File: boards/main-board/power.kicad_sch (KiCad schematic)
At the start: 18 parts, among them U3 LM317

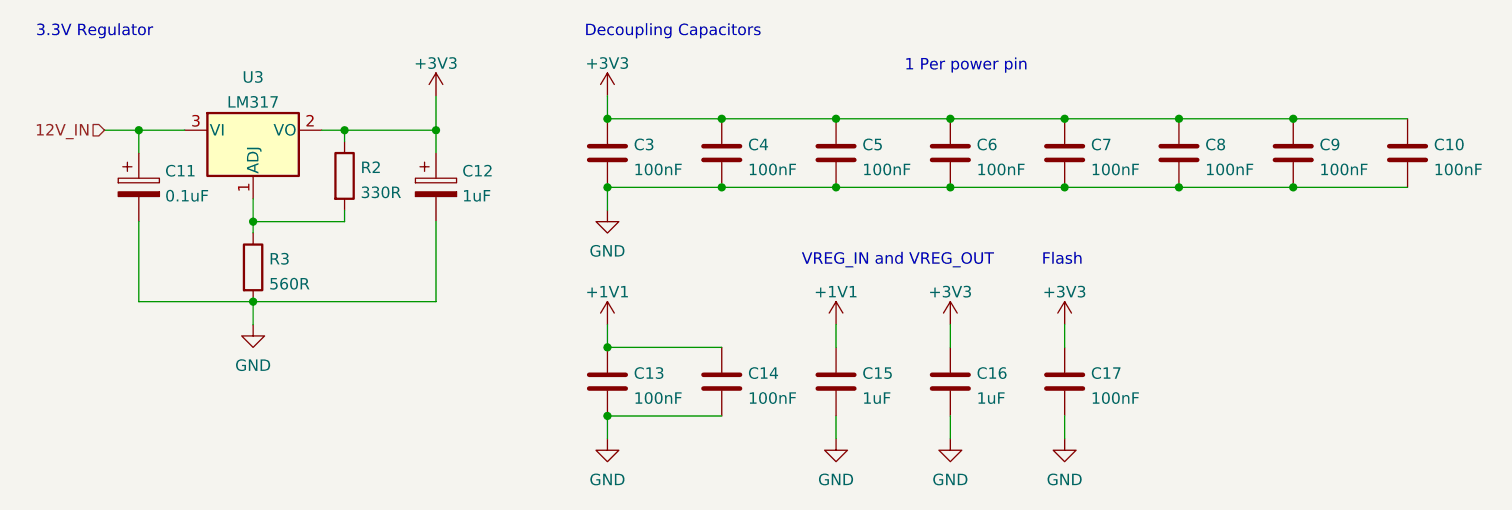
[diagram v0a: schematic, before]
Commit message: Version 1.1.0 of main control board schematic
Signed-off-by: Computroniks <mnickson@sidingsmedia.com>
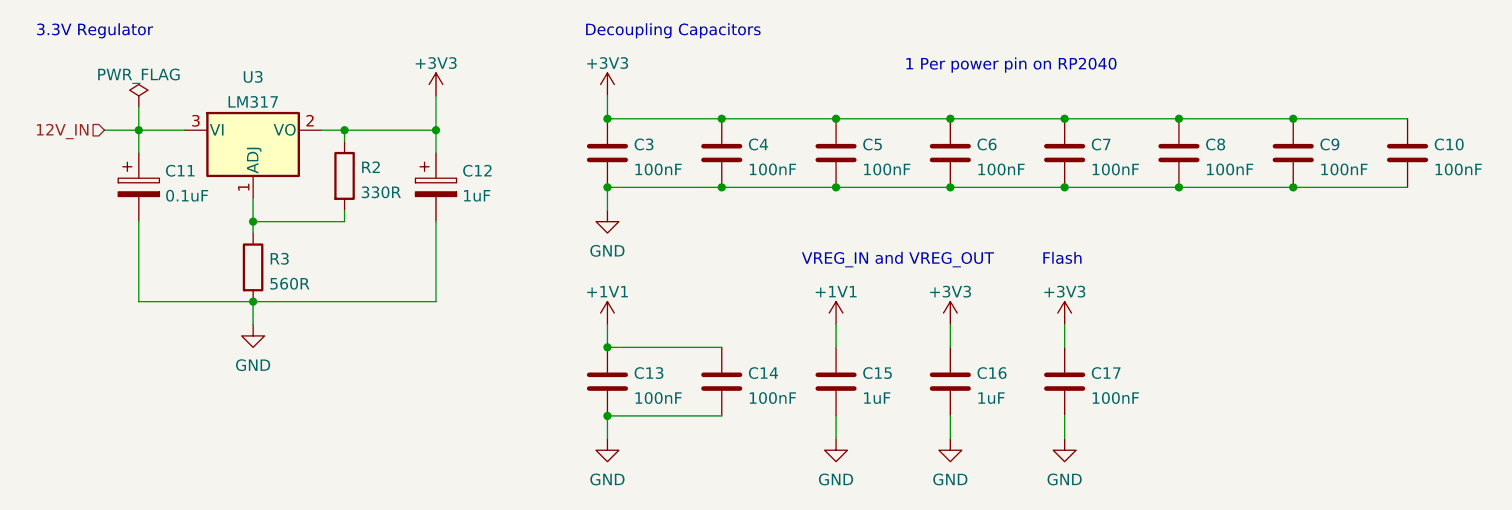
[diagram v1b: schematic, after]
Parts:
- C10, C13, C14, C15, C16, C17, C3, C4, C5, C6, C7, C8, C9: footprint (none) -> Capacitor_SMD:C_0805_2012Metric
- C11, C12: footprint (none) -> Capacitor_SMD:CP_Elec_4x3
- R2, R3: footprint (none) -> Resistor_SMD:R_0805_2012Metric
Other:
- note added: "1 Per power pin on RP2040"
- note removed: "1 Per power pin"
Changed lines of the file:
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@@
   (title_block
     (title "Main Board")
-    (date "2022-01-02")
-    (rev "V1.0.0")
+    (date "2022-03-18")
+    (rev "V1.1.0")
     (company "Matthew Nickson")
     (comment 1 "Licence: CC-BY-SA-4.0")
@@
     (stroke (width 0) (type default) (color 0 0 0 0))
   )
+  (wire (pts (xy 26.67 22.86) (xy 26.67 25.4))
+    (stroke (width 0) (type default) (color 0 0 0 0))
+  )
   (wire (pts (xy 22.86 25.4) (xy 26.67 25.4))
     (stroke (width 0) (type default) (color 0 0 0 0))
@@
     (effects (font (size 1.27 1.27)) (justify left bottom))
   )
-  (text "1 Per power pin" (at 111.76 19.05 0)
+  (text "1 Per power pin on RP2040" (at 111.76 19.05 0)
     (effects (font (size 1.27 1.27)) (justify left bottom))
   )
@@
       (effects (font (size 1.27 1.27)) (justify left))
     )
-    (property "Footprint" "" (id 2) (at 27.6352 35.56 0)
+    (property "Footprint" "Capacitor_SMD:CP_Elec_4x3" (id 2) (at 27.6352 35.56 0)
       (effects (font (size 1.27 1.27)) hide)
     )
@@
       (effects (font (size 1.27 1.27)) (justify left))
     )
-    (property "Footprint" "" (id 2) (at 168.6052 31.75 0)
+    (property "Footprint" "Capacitor_SMD:C_0805_2012Metric" (id 2) (at 168.6052 31.75 0)
       (effects (font (size 1.27 1.27)) hide)
     )
@@
       (effects (font (size 1.27 1.27)) (justify left))
     )
-    (property "Footprint" "" (id 2) (at 92.4052 31.75 0)
+    (property "Footprint" "Capacitor_SMD:C_0805_2012Metric" (id 2) (at 92.4052 31.75 0)
       (effects (font (size 1.27 1.27)) hide)
     )
@@
       (effects (font (size 1.27 1.27)) (justify left))
     )
-    (property "Footprint" "" (id 2) (at 117.8052 57.15 0)
+    (property "Footprint" "Capacitor_SMD:C_0805_2012Metric" (id 2) (at 117.8052 57.15 0)
       (effects (font (size 1.27 1.27)) hide)
     )
@@
       (effects (font (size 1.27 1.27)) (justify left))
     )
-    (property "Footprint" "" (id 2) (at 143.2052 31.75 0)
+    (property "Footprint" "Capacitor_SMD:C_0805_2012Metric" (id 2) (at 143.2052 31.75 0)
       (effects (font (size 1.27 1.27)) hide)
     )
@@
       (effects (font (size 1.27 1.27)) (justify left))
     )
-    (property "Footprint" "" (id 2) (at 92.4052 57.15 0)
+    (property "Footprint" "Capacitor_SMD:C_0805_2012Metric" (id 2) (at 92.4052 57.15 0)
       (effects (font (size 1.27 1.27)) hide)
     )
@@
       (effects (font (size 1.27 1.27)) (justify left))
     )
-    (property "Footprint" "" (id 2) (at 130.5052 31.75 0)
+    (property "Footprint" "Capacitor_SMD:C_0805_2012Metric" (id 2) (at 130.5052 31.75 0)
       (effects (font (size 1.27 1.27)) hide)
     )
@@
       (effects (font (size 1.27 1.27)) (justify left))
     )
-    (property "Footprint" "" (id 2) (at 105.1052 57.15 0)
+    (property "Footprint" "Capacitor_SMD:C_0805_2012Metric" (id 2) (at 105.1052 57.15 0)
       (effects (font (size 1.27 1.27)) hide)
     )
@@
       (effects (font (size 1.27 1.27)) (justify left))
     )
-    (property "Footprint" "" (id 2) (at 37.592 40.64 90)
+    (property "Footprint" "Resistor_SMD:R_0805_2012Metric" (id 2) (at 37.592 40.64 90)
       (effects (font (size 1.27 1.27)) hide)
     )
@@
       (effects (font (size 1.27 1.27)) (justify left))
     )
-    (property "Footprint" "" (id 2) (at 60.6552 35.56 0)
+    (property "Footprint" "Capacitor_SMD:CP_Elec_4x3" (id 2) (at 60.6552 35.56 0)
       (effects (font (size 1.27 1.27)) hide)
     )
@@
       (effects (font (size 1.27 1.27)) (justify left))
     )
-    (property "Footprint" "" (id 2) (at 130.5052 57.15 0)
+    (property "Footprint" "Capacitor_SMD:C_0805_2012Metric" (id 2) (at 130.5052 57.15 0)
       (effects (font (size 1.27 1.27)) hide)
     )
@@
       (effects (font (size 1.27 1.27)) (justify left))
     )
-    (property "Footprint" "" (id 2) (at 47.752 30.48 90)
+    (property "Footprint" "Resistor_SMD:R_0805_2012Metric" (id 2) (at 47.752 30.48 90)
       (effects (font (size 1.27 1.27)) hide)
     )
@@
       (effects (font (size 1.27 1.27)) (justify left))
     )
-    (property "Footprint" "" (id 2) (at 105.1052 31.75 0)
+    (property "Footprint" "Capacitor_SMD:C_0805_2012Metric" (id 2) (at 105.1052 31.75 0)
       (effects (font (size 1.27 1.27)) hide)
     )
@@
       (effects (font (size 1.27 1.27)) (justify left))
     )
-    (property "Footprint" "" (id 2) (at 79.7052 57.15 0)
+    (property "Footprint" "Capacitor_SMD:C_0805_2012Metric" (id 2) (at 79.7052 57.15 0)
       (effects (font (size 1.27 1.27)) hide)
     )
@@
     (pin "2")
   )
+  (symbol (lib_id "power:PWR_FLAG") (at 26.67 22.86 0) (unit 1)
+    (in_bom yes) (on_board yes) (fields_autoplaced)
+    (property "Reference" "#FLG0101" (id 0) (at 26.67 20.955 0)
+      (effects (font (size 1.27 1.27)) hide)
+    )
+    (property "Value" "PWR_FLAG" (id 1) (at 26.67 19.2555 0))
+    (property "Footprint" "" (id 2) (at 26.67 22.86 0)
+      (effects (font (size 1.27 1.27)) hide)
+    )
+    (property "Datasheet" "~" (id 3) (at 26.67 22.86 0)
+      (effects (font (size 1.27 1.27)) hide)
+    )
+    (pin "1")
+  )
   (symbol (lib_id "Device:C") (at 78.74 27.94 0) (unit 1)
     (in_bom yes) (on_board yes) (fields_autoplaced)
@@
       (effects (font (size 1.27 1.27)) (justify left))
     )
-    (property "Footprint" "" (id 2) (at 79.7052 31.75 0)
+    (property "Footprint" "Capacitor_SMD:C_0805_2012Metric" (id 2) (at 79.7052 31.75 0)
       (effects (font (size 1.27 1.27)) hide)
     )
@@
       (effects (font (size 1.27 1.27)) (justify left))
     )
-    (property "Footprint" "" (id 2) (at 155.9052 31.75 0)
+    (property "Footprint" "Capacitor_SMD:C_0805_2012Metric" (id 2) (at 155.9052 31.75 0)
       (effects (font (size 1.27 1.27)) hide)
     )
@@
       (effects (font (size 1.27 1.27)) (justify left))
     )
-    (property "Footprint" "" (id 2) (at 117.8052 31.75 0)
-      (effects (font (size 1.27 1.27)) hide)
-    )
+    (property "Footprint" "Capacitor_SMD:C_0805_2012Metric" (id 2) (at 117.8052 31.75 0)
+      (effects (font (size 1.27 1.27)) hide)
+    )
